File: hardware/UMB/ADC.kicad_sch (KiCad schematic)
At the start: 4 parts, among them U2 ADS114S08BIPBSR

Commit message: Power section done
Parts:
- C2, C4: footprint Capacitor_SMD:C_0603_1608Metric -> Capacitor_SMD:C_0603_1608Metric_Pad1.08x0.95mm_HandSolder; Mouser (none) -> https://www.mouser.pl/ProductDetail/KEMET/C0603C104M4RACAUT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; Mouser No (none) -> 80-C0603C104M4RAUTO
- C3: Mouser (none) -> https://www.mouser.pl/ProductDetail/KEMET/C0603C105K4RACTU?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; Mouser No (none) -> 80-C0603C105K4R
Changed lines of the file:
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@@
 		(on_board yes)
 		(dnp no)
-		(property "Reference" "#PWR016"
+		(property "Reference" "#PWR05"
 			(at 185.42 80.01 0)
 			(effects
@@
 			(project "UMB"
 				(path "/b652b05a-4e3d-4ad1-b032-18886abe7d45/27728c5b-995e-4e9b-804c-adae9f98b692"
-					(reference "#PWR016")
+					(reference "#PWR05")
 					(unit 1)
 				)
@@
 			)
 		)
-		(property "Footprint" "Capacitor_SMD:C_0603_1608Metric"
+		(property "Footprint" "Capacitor_SMD:C_0603_1608Metric_Pad1.08x0.95mm_HandSolder"
 			(at 156.21 130.81 0)
 			(effects
@@
 			)
 		)
-		(property "Datasheet" "~"
+		(property "Datasheet" "https://www.mouser.pl/datasheet/3/72/1/C0603C104M4RACAUTO.pdf"
 			(at 156.21 130.81 0)
 			(effects
@@
 			)
 		)
-		(property "Description" "Unpolarized capacitor, small symbol"
+		(property "Description" "Unpolarized capacitor"
+			(at 156.21 130.81 0)
+			(effects
+				(font
+					(size 1.27 1.27)
+				)
+				(hide yes)
+			)
+		)
+		(property "Sim.Device" ""
+			(at 156.21 130.81 0)
+			(effects
+				(font
+					(size 1.27 1.27)
+				)
+				(hide yes)
+			)
+		)
+		(property "Sim.Library" ""
+			(at 156.21 130.81 0)
+			(effects
+				(font
+					(size 1.27 1.27)
+				)
+				(hide yes)
+			)
+		)
+		(property "Sim.Name" ""
+			(at 156.21 130.81 0)
+			(effects
+				(font
+					(size 1.27 1.27)
+				)
+				(hide yes)
+			)
+		)
+		(property "Sim.Pins" ""
+			(at 156.21 130.81 0)
+			(effects
+				(font
+					(size 1.27 1.27)
+				)
+				(hide yes)
+			)
+		)
+		(property "Mouser" "https://www.mouser.pl/ProductDetail/KEMET/C0603C104M4RACAUTO?qs=sSYV1F9c5cFMyVgVMlPozw%3D%3D"
+			(at 156.21 130.81 0)
+			(effects
+				(font
+					(size 1.27 1.27)
+				)
+				(hide yes)
+			)
+		)
+		(property "Mouser No" "80-C0603C104M4RAUTO"
 			(at 156.21 130.81 0)
 			(effects
@@
 		(on_board yes)
 		(dnp no)
-		(property "Reference" "#PWR02"
+		(property "Reference" "#PWR06"
 			(at 121.92 87.63 0)
 			(effects
@@
 			(project "UMB"
 				(path "/b652b05a-4e3d-4ad1-b032-18886abe7d45/27728c5b-995e-4e9b-804c-adae9f98b692"
-					(reference "#PWR02")
+					(reference "#PWR06")
 					(unit 1)
 				)
@@
 			)
 		)
+		(property "Sim.Device" ""
+			(at 124.46 81.28 0)
+			(effects
+				(font
+					(size 1.27 1.27)
+				)
+				(hide yes)
+			)
+		)
+		(property "Sim.Library" ""
+			(at 124.46 81.28 0)
+			(effects
+				(font
+					(size 1.27 1.27)
+				)
+				(hide yes)
+			)
+		)
+		(property "Sim.Name" ""
+			(at 124.46 81.28 0)
+			(effects
+				(font
+					(size 1.27 1.27)
+				)
+				(hide yes)
+			)
+		)
+		(property "Sim.Pins" ""
+			(at 124.46 81.28 0)
+			(effects
+				(font
+					(size 1.27 1.27)
+				)
+				(hide yes)
+			)
+		)
 		(pin "8"
 		)
@@
 		(on_board yes)
 		(dnp no)
-		(property "Reference" "#PWR01"
+		(property "Reference" "#PWR08"
 			(at 160.02 129.54 0)
 			(effects
@@
 			(project "UMB"
 				(path "/b652b05a-4e3d-4ad1-b032-18886abe7d45/27728c5b-995e-4e9b-804c-adae9f98b692"
-					(reference "#PWR01")
+					(reference "#PWR08")
 					(unit 1)
 				)
@@
 		(dnp no)
 		(fields_autoplaced yes)
-		(property "Reference" "#FLG02"
+		(property "Reference" "#FLG01"
 			(at 116.205 78.74 0)
 			(effects
@@
 			(project "UMB"
 				(path "/b652b05a-4e3d-4ad1-b032-18886abe7d45/27728c5b-995e-4e9b-804c-adae9f98b692"
-					(reference "#FLG02")
+					(reference "#FLG01")
 					(unit 1)
 				)
@@
 		(on_board yes)
 		(dnp no)
-		(property "Reference" "#PWR017"
+		(property "Reference" "#PWR07"
 			(at 171.45 116.84 0)
 			(effects
@@
 			(project "UMB"
 				(path "/b652b05a-4e3d-4ad1-b032-18886abe7d45/27728c5b-995e-4e9b-804c-adae9f98b692"
-					(reference "#PWR017")
+					(reference "#PWR07")
 					(unit 1)
 				)
@@
 			)
 		)
-		(property "Datasheet" "~"
+		(property "Datasheet" "https://www.mouser.pl/datasheet/3/72/1/C0603C105K4RACTU.pdf"
 			(at 177.8 74.93 0)
 			(effects
@@
 		)
 		(property "Description" "Unpolarized capacitor"
+			(at 177.8 74.93 0)
+			(effects
+				(font
+					(size 1.27 1.27)
+				)
+				(hide yes)
+			)
+		)
+		(property "Sim.Device" ""
+			(at 177.8 74.93 0)
+			(effects
+				(font
+					(size 1.27 1.27)
+				)
+				(hide yes)
+			)
+		)
+		(property "Sim.Library" ""
+			(at 177.8 74.93 0)
+			(effects
+				(font
+					(size 1.27 1.27)
+				)
+				(hide yes)
+			)
+		)
+		(property "Sim.Name" ""
+			(at 177.8 74.93 0)
+			(effects
+				(font
+					(size 1.27 1.27)
+				)
+				(hide yes)
+			)
+		)
+		(property "Sim.Pins" ""
+			(at 177.8 74.93 0)
+			(effects
+				(font
+					(size 1.27 1.27)
+				)
+				(hide yes)
+			)
+		)
+		(property "Mouser" "https://www.mouser.pl/ProductDetail/KEMET/C0603C105K4RACTU?qs=STjISULpmtZNMAZGR4X39Q%3D%3D"
+			(at 177.8 74.93 0)
+			(effects
+				(font
+					(size 1.27 1.27)
+				)
+				(hide yes)
+			)
+		)
+		(property "Mouser No" "80-C0603C105K4R"
 			(at 177.8 74.93 0)
 			(effects
@@
 		(on_board yes)
 		(dnp no)
-		(property "Reference" "#PWR044"
+		(property "Reference" "#PWR09"
 			(at 151.13 139.7 0)
 			(effects
@@
 			(project "UMB"
 				(path "/b652b05a-4e3d-4ad1-b032-18886abe7d45/27728c5b-995e-4e9b-804c-adae9f98b692"
-					(reference "#PWR044")
+					(reference "#PWR09")
 					(unit 1)
 				)
@@
 			)
 		)
-		(property "Footprint" "Capacitor_SMD:C_0603_1608Metric"
+		(property "Footprint" "Capacitor_SMD:C_0603_1608Metric_Pad1.08x0.95mm_HandSolder"
 			(at 118.11 74.93 0)
 			(effects
@@
 			)
 		)
-		(property "Datasheet" "~"
+		(property "Datasheet" "https://www.mouser.pl/datasheet/3/72/1/C0603C104M4RACAUTO.pdf"
 			(at 118.11 74.93 0)
 			(effects
@@
 			)
 		)
-		(property "Description" "Unpolarized capacitor, small symbol"
+		(property "Description" "Unpolarized capacitor"
+			(at 118.11 74.93 0)
+			(effects
+				(font
+					(size 1.27 1.27)
+				)
+				(hide yes)
+			)
+		)
+		(property "Sim.Device" ""
+			(at 118.11 74.93 0)
+			(effects
+				(font
+					(size 1.27 1.27)
+				)
+				(hide yes)
+			)
+		)
+		(property "Sim.Library" ""
+			(at 118.11 74.93 0)
+			(effects
+				(font
+					(size 1.27 1.27)
+				)
+				(hide yes)
+			)
+		)
+		(property "Sim.Name" ""
+			(at 118.11 74.93 0)
+			(effects
+				(font
+					(size 1.27 1.27)
+				)
+				(hide yes)
+			)
+		)
+		(property "Sim.Pins" ""
+			(at 118.11 74.93 0)
+			(effects
+				(font
+					(size 1.27 1.27)
+				)
+				(hide yes)
+			)
+		)
+		(property "Mouser" "https://www.mouser.pl/ProductDetail/KEMET/C0603C104M4RACAUTO?qs=sSYV1F9c5cFMyVgVMlPozw%3D%3D"
+			(at 118.11 74.93 0)
+			(effects
+				(font
+					(size 1.27 1.27)
+				)
+				(hide yes)
+			)
+		)
+		(property "Mouser No" "80-C0603C104M4RAUTO"
 			(at 118.11 74.93 0)
 			(effects
@@
 		(dnp no)
 		(fields_autoplaced yes)
-		(property "Reference" "#PWR015"
+		(property "Reference" "#PWR04"
 			(at 118.11 74.93 0)
 			(effects
@@
 			(project "UMB"
 				(path "/b652b05a-4e3d-4ad1-b032-18886abe7d45/27728c5b-995e-4e9b-804c-adae9f98b692"
-					(reference "#PWR015")
+					(reference "#PWR04")
 					(unit 1)
 				)

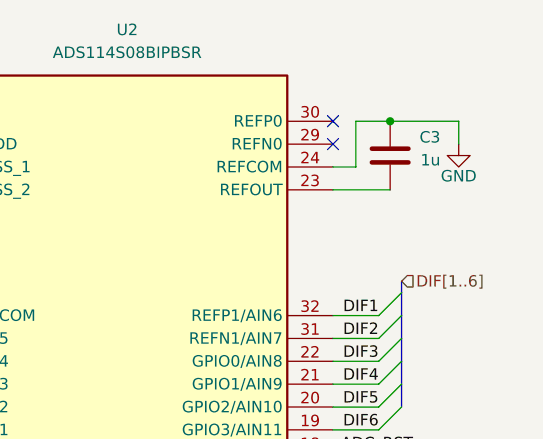
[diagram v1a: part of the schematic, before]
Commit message: Added all footprints and parts Mouser IDs
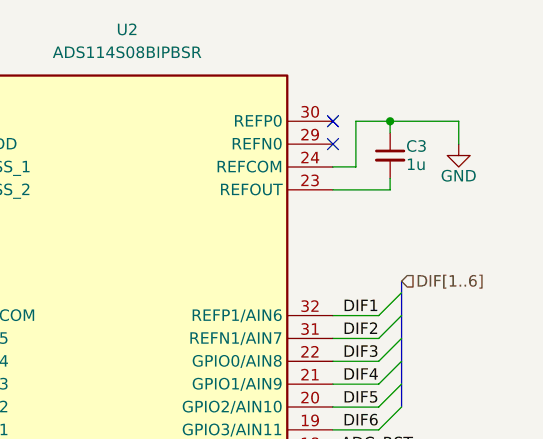
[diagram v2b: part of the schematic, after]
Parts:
- removed C3: 1u, Capacitor_SMD:C_0603_1608Metric_Pad1.08x0.95mm_HandSolder, symbol Device:C
- added C3: 1u, Capacitor_SMD:C_0603_1608Metric_Pad1.08x0.95mm_HandSolder, symbol Device:C_Small
- C2, C4: Manufacturer_Part_Number (none) -> C0603C104M4RACAUTO
- U2: Height 1.2 -> (none); Manufacturer_Name Texas Instruments -> (none); Mouser (none) -> https://www.mouser.pl/ProductDetail/Texas-Instruments/ADS11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; Mouser No (none) -> 595-ADS114S08BIPBSR; Mouser Part Number 595-ADS114S08BIPBSR -> (none); Mouser Price/Stock https://www.mouser.co.uk/ProductDetail/Texas-Instruments/AD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 -> (none)
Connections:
- net GND: now also C3.1
- net at U2.23 (REFOUT): now also C3.2
